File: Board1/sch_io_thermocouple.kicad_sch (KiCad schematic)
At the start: 6 parts, among them J3 Thermo, U3 MAX31855KASA

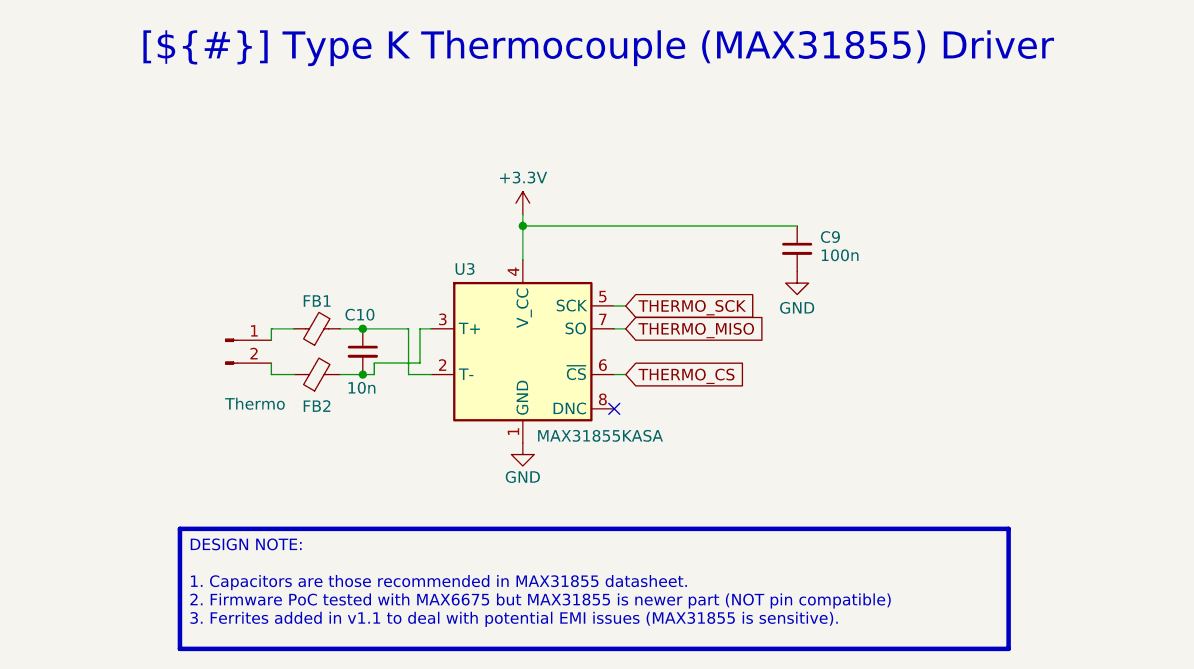
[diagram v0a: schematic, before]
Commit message: Resolve library and ERC issues
No changes to design.
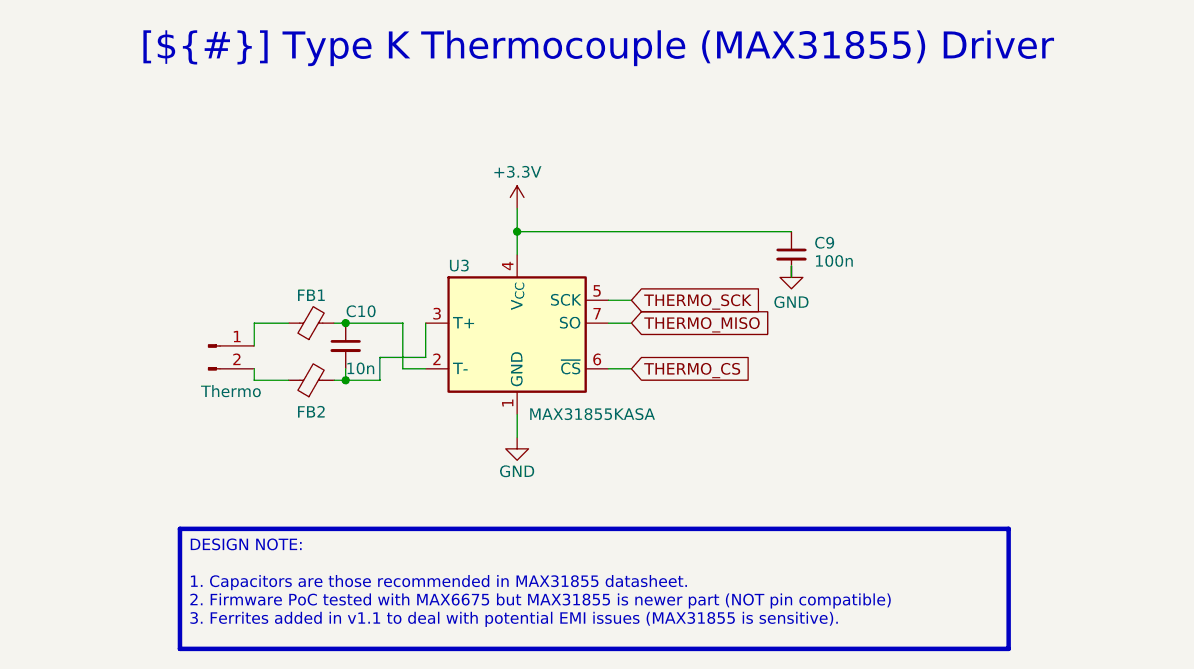
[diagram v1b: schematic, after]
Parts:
- U3: Digikey_PN MAX31855KASA+-ND -> (none); Supplier https://www.digikey.co.nz/en/products/detail/analog-devices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 -> (none)
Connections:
- no-connect marks 1 -> 0
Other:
- moved on the sheet: C10, C9, FB1, FB2
